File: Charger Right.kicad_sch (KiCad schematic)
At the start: 21 parts, among them J2 BRAUNIT, Q3 AO4459, Q4 2N7002, U2 CN3702

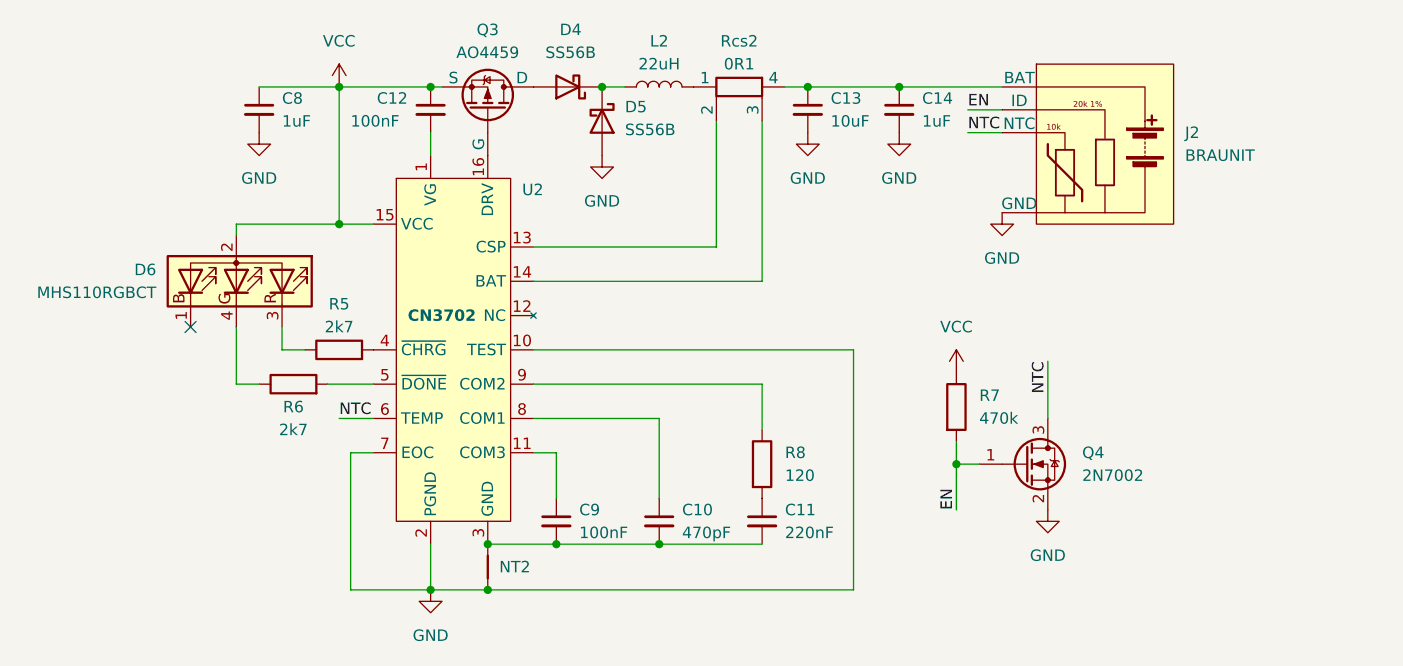
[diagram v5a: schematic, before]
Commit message: Add ESD protection, I2C header, and specify passives
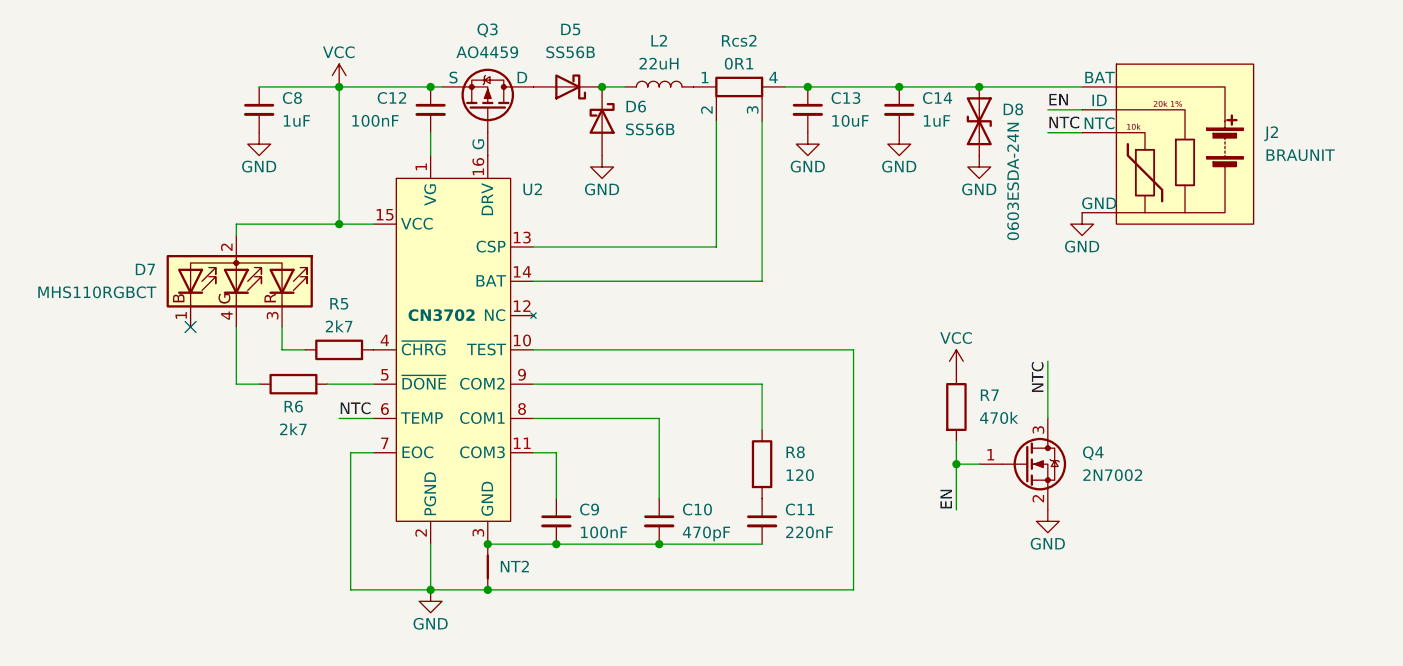
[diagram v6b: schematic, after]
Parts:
- added D8: 0603ESDA-24N, Diode_SMD:D_0603_1608Metric, symbol Device:D_TVS
- C11: footprint Capacitor_SMD:C_0805_2012Metric -> Capacitor_SMD:C_0603_1608Metric; LCSC C107131 -> C107083
- C12, C9: footprint Capacitor_SMD:C_0805_2012Metric -> Capacitor_SMD:C_0603_1608Metric; LCSC C49678 -> C14663
- R7: footprint Resistor_SMD:R_0805_2012Metric -> Resistor_SMD:R_0603_1608Metric; LCSC C89104 -> C114622
- R8: footprint Resistor_SMD:R_0805_2012Metric -> Resistor_SMD:R_0603_1608Metric; LCSC C114245 -> C114640
- renumbered D4 to D5, D5 to D6, D6 to D7
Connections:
- net GND: now also D8.2 (A2)
- net at C13.1, C14.1, J2.1 (BAT)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: now also D8.1 (A1)
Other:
- moved on the sheet: J2

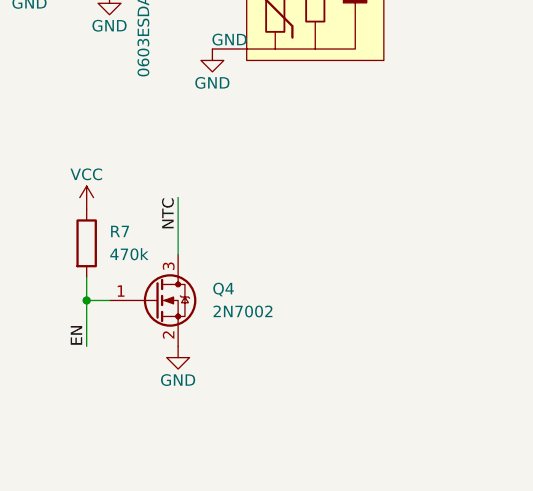
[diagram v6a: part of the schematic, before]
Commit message: Add USB-C status indicator LED and right charger enable
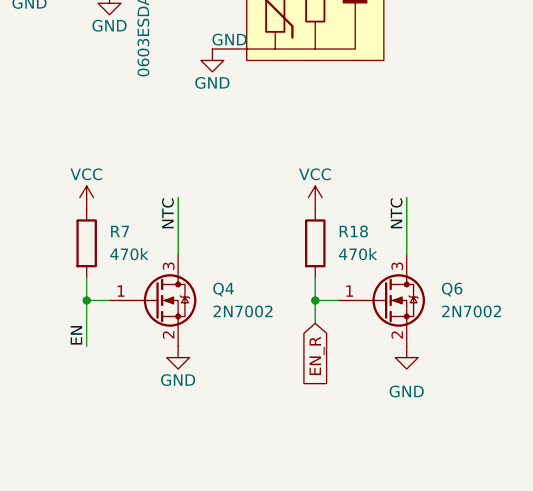
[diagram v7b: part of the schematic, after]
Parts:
- added Q6: 2N7002, Package_TO_SOT_SMD:SOT-23, symbol Transistor_FET:2N7002
- added R18: 470k, Resistor_SMD:R_0603_1608Metric, symbol Device:R
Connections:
- net GND: now also Q6.2 (S)
- net NTC: now also Q6.3 (D)
- net VCC: now also R18.1
- new net EN_R: Q6.1 (G), R18.2
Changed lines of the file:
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@@
   (junction (at 138.43 123.19) (diameter 0) (color 0 0 0 0)
+  )
+  (junction (at 208.28 114.3) (diameter 0) (color 0 0 0 0)
   )
   (junction (at 185.42 72.39) (diameter 0) (color 0 0 0 0)
@@
     (stroke (width 0) (type default) (color 0 0 0 0))
   )
+  (wire (pts (xy 208.28 114.3) (xy 210.82 114.3))
+    (stroke (width 0) (type default) (color 0 0 0 0))
+  )
   (wire (pts (xy 156.21 76.2) (xy 156.21 90.17))
     (stroke (width 0) (type default) (color 0 0 0 0))
@@
     (stroke (width 0) (type default) (color 0 0 0 0))
   )
+  (wire (pts (xy 218.44 102.87) (xy 218.44 109.22))
+    (stroke (width 0) (type default) (color 0 0 0 0))
+  )
+  (wire (pts (xy 208.28 111.76) (xy 208.28 114.3))
+    (stroke (width 0) (type default) (color 0 0 0 0))
+  )
   (wire (pts (xy 149.86 118.11) (xy 149.86 109.22))
     (stroke (width 0) (type default) (color 0 0 0 0))
@@
   )
   (wire (pts (xy 138.43 113.03) (xy 135.89 113.03))
+    (stroke (width 0) (type default) (color 0 0 0 0))
+  )
+  (wire (pts (xy 208.28 114.3) (xy 208.28 116.84))
     (stroke (width 0) (type default) (color 0 0 0 0))
   )
@@
     (effects (font (size 1.27 1.27)) (justify left bottom))
   )
+  (label "NTC" (at 218.44 102.87 270)
+    (effects (font (size 1.27 1.27)) (justify right bottom))
+  )
   (label "NTC" (at 193.04 77.47 0)
     (effects (font (size 1.27 1.27)) (justify left bottom))
+  )
+  (global_label "EN_R" (shape input) (at 208.28 116.84 270) (fields_autoplaced)
+    (effects (font (size 1.27 1.27)) (justify right))
+    (property "Intersheet References" "${INTERSHEET_REFS}" (id 0) (at 208.2006 123.9702 90)
+      (effects (font (size 1.27 1.27)) (justify right) hide)
+    )
+  )
+  (symbol (lib_id "power:VCC") (at 208.28 104.14 0) (unit 1)
+    (in_bom yes) (on_board yes)
+    (property "Reference" "#PWR0135" (id 0) (at 208.28 107.95 0)
+      (effects (font (size 1.27 1.27)) hide)
+    )
+    (property "Value" "VCC" (id 1) (at 208.28 100.33 0))
+    (property "Footprint" "" (id 2) (at 208.28 104.14 0)
+      (effects (font (size 1.27 1.27)) hide)
+    )
+    (property "Datasheet" "" (id 3) (at 208.28 104.14 0)
+      (effects (font (size 1.27 1.27)) hide)
+    )
+    (pin "1")
   )
   (symbol (lib_id "power:GND") (at 143.51 80.01 0) (unit 1)
@@
     (pin "2")
   )
+  (symbol (lib_id "Device:R") (at 208.28 107.95 0) (unit 1)
+    (in_bom yes) (on_board yes) (fields_autoplaced)
+    (property "Reference" "R18" (id 0) (at 210.82 106.6799 0)
+      (effects (font (size 1.27 1.27)) (justify left))
+    )
+    (property "Value" "470k" (id 1) (at 210.82 109.2199 0)
+      (effects (font (size 1.27 1.27)) (justify left))
+    )
+    (property "Footprint" "Resistor_SMD:R_0603_1608Metric" (id 2) (at 206.502 107.95 90)
+      (effects (font (size 1.27 1.27)) hide)
+    )
+    (property "Datasheet" "~" (id 3) (at 208.28 107.95 0)
+      (effects (font (size 1.27 1.27)) hide)
+    )
+    (property "LCSC" "C114622" (id 4) (at 208.28 107.95 0)
+      (effects (font (size 1.27 1.27)) hide)
+    )
+    (pin "1")
+    (pin "2")
+  )
   (symbol (lib_id "power:GND") (at 185.42 80.01 0) (unit 1)
     (in_bom yes) (on_board yes)
@@
     (pin "3")
   )
+  (symbol (lib_id "Transistor_FET:2N7002") (at 215.9 114.3 0) (unit 1)
+    (in_bom yes) (on_board yes) (fields_autoplaced)
+    (property "Reference" "Q6" (id 0) (at 222.25 113.0299 0)
+      (effects (font (size 1.27 1.27)) (justify left))
+    )
+    (property "Value" "2N7002" (id 1) (at 222.25 115.5699 0)
+      (effects (font (size 1.27 1.27)) (justify left))
+    )
+    (property "Footprint" "Package_TO_SOT_SMD:SOT-23" (id 2) (at 220.98 116.205 0)
+      (effects (font (size 1.27 1.27) italic) (justify left) hide)
+    )
+    (property "Datasheet" "https://www.onsemi.com/pub/Collateral/NDS7002A-D.PDF" (id 3) (at 215.9 114.3 0)
+      (effects (font (size 1.27 1.27)) (justify left) hide)
+    )
+    (property "LCSC" "C8545" (id 4) (at 215.9 114.3 0)
+      (effects (font (size 1.27 1.27)) hide)
+    )
+    (pin "1")
+    (pin "2")
+    (pin "3")
+  )
   (symbol (lib_id "Device:D_Schottky") (at 143.51 76.2 270) (unit 1)
     (in_bom yes) (on_board yes) (fields_autoplaced)
@@
     (pin "2")
   )
+  (symbol (lib_id "power:GND") (at 218.44 119.38 0) (unit 1)
+    (in_bom yes) (on_board yes) (fields_autoplaced)
+    (property "Reference" "#PWR0136" (id 0) (at 218.44 125.73 0)
+      (effects (font (size 1.27 1.27)) hide)
+    )
+    (property "Value" "GND" (id 1) (at 218.44 124.46 0))
+    (property "Footprint" "" (id 2) (at 218.44 119.38 0)
+      (effects (font (size 1.27 1.27)) hide)
+    )
+    (property "Datasheet" "" (id 3) (at 218.44 119.38 0)
+      (effects (font (size 1.27 1.27)) hide)
+    )
+    (pin "1")
+  )
   (symbol (lib_id "Device:C_Small") (at 161.29 120.65 0) (unit 1)

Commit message: Initial board layout
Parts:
- L2: footprint Inductor_SMD:L_10.4x10.4_H4.8 -> BRAUNIT Charger:L_Sunltech_SLO0630H; LCSC C182173 -> C207843
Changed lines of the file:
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@@
     (property "Reference" "L2" (id 0) (at 149.86 67.31 90))
     (property "Value" "22uH" (id 1) (at 149.86 69.85 90))
-    (property "Footprint" "Inductor_SMD:L_10.4x10.4_H4.8" (id 2) (at 149.86 72.39 0)
+    (property "Footprint" "BRAUNIT Charger:L_Sunltech_SLO0630H" (id 2) (at 149.86 72.39 0)
       (effects (font (size 1.27 1.27)) hide)
     )
@@
       (effects (font (size 1.27 1.27)) hide)
     )
-    (property "LCSC" "C182173" (id 4) (at 149.86 72.39 90)
+    (property "LCSC" "C207843" (id 4) (at 149.86 72.39 90)
       (effects (font (size 1.27 1.27)) hide)
     )
